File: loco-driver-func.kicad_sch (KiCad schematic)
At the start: 5 parts, among them Q901 BSS138, Q902 BSS138

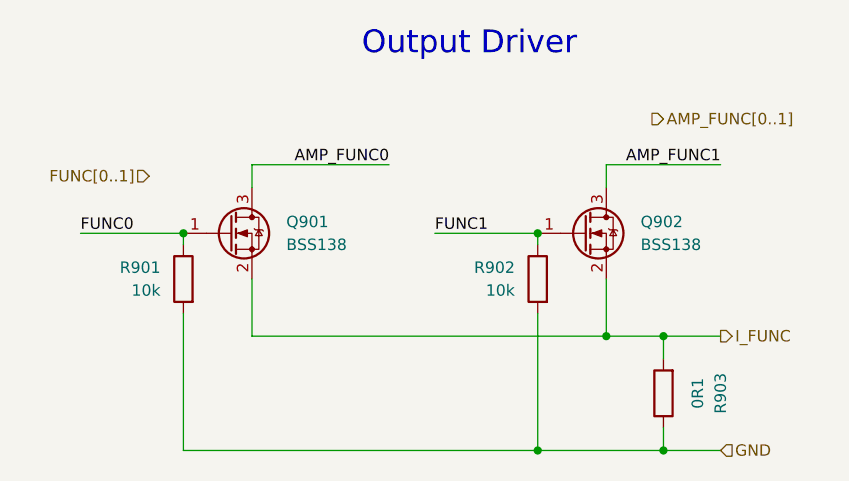
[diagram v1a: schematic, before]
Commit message: Fix - loco-driver-func (ERC)
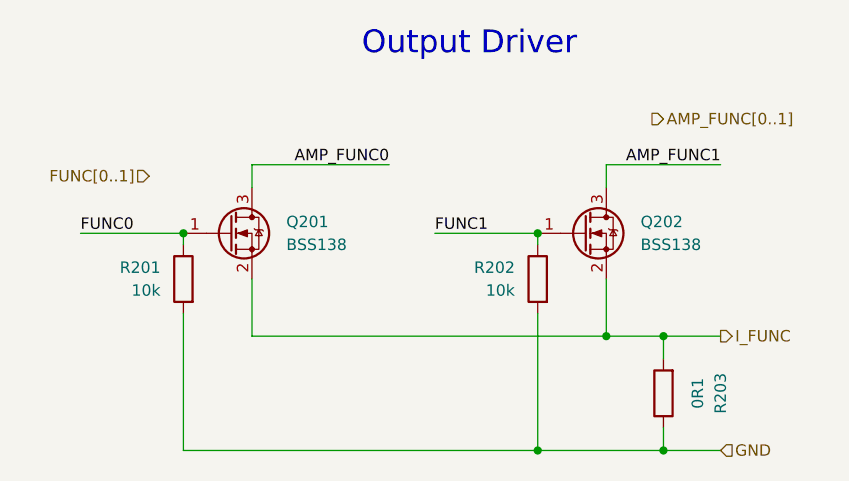
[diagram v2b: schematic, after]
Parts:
- renumbered Q901 to Q201, Q902 to Q202, R901 to R201, R902 to R202, R903 to R203
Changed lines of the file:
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@@
 		(on_board yes)
 		(dnp no)
-		(property "Reference" "R902"
+		(property "Reference" "R202"
 			(at 76.2 59.6899 0)
 			(effects
@@
 			)
 		)
+		(property "Sim.Type" ""
+			(at 78.74 60.96 0)
+			(effects
+				(font
+					(size 1.27 1.27)
+				)
+				(hide yes)
+			)
+		)
 		(pin "2"
 		)
@@
 		)
 		(instances
+			(project "loco-driver-func-test"
+				(path "/05e300d5-f5fa-4357-9552-f348c65b0d1e/d4f38dff-3059-4603-8995-2402d29cae24"
+					(reference "R202")
+					(unit 1)
+				)
+			)
 			(project "xDuinoRails-Thor-M"
 				(path "/fb33ec4e-6596-45d2-a121-8d3475acd69a/e1a52612-70a7-429e-ada6-6f2a698a279c"
@@
 		(on_board yes)
 		(dnp no)
-		(property "Reference" "R903"
+		(property "Reference" "R203"
 			(at 99.06 73.66 90)
 			(effects
@@
 			)
 		)
+		(property "Sim.Type" ""
+			(at 92.71 73.66 0)
+			(effects
+				(font
+					(size 1.27 1.27)
+				)
+				(hide yes)
+			)
+		)
 		(pin "2"
 		)
@@
 		)
 		(instances
+			(project "loco-driver-func-test"
+				(path "/05e300d5-f5fa-4357-9552-f348c65b0d1e/d4f38dff-3059-4603-8995-2402d29cae24"
+					(reference "R203")
+					(unit 1)
+				)
+			)
 			(project "xDuinoRails-Thor-M"
 				(path "/fb33ec4e-6596-45d2-a121-8d3475acd69a/e1a52612-70a7-429e-ada6-6f2a698a279c"
@@
 		(on_board yes)
 		(dnp no)
-		(property "Reference" "R901"
+		(property "Reference" "R201"
 			(at 36.83 59.6899 0)
 			(effects
@@
 			)
 		)
+		(property "Sim.Type" ""
+			(at 39.37 60.96 0)
+			(effects
+				(font
+					(size 1.27 1.27)
+				)
+				(hide yes)
+			)
+		)
 		(pin "2"
 		)
@@
 		)
 		(instances
+			(project "loco-driver-func-test"
+				(path "/05e300d5-f5fa-4357-9552-f348c65b0d1e/d4f38dff-3059-4603-8995-2402d29cae24"
+					(reference "R201")
+					(unit 1)
+				)
+			)
 			(project "xDuinoRails-Thor-M"
 				(path "/fb33ec4e-6596-45d2-a121-8d3475acd69a/e1a52612-70a7-429e-ada6-6f2a698a279c"
@@
 		(dnp no)
 		(fields_autoplaced yes)
-		(property "Reference" "Q901"
+		(property "Reference" "Q201"
 			(at 50.8 54.6099 0)
 			(effects
@@
 			)
 		)
+		(property "Sim.Type" ""
+			(at 44.45 55.88 0)
+			(effects
+				(font
+					(size 1.27 1.27)
+				)
+				(hide yes)
+			)
+		)
 		(pin "1"
 		)
@@
 		)
 		(instances
+			(project "loco-driver-func-test"
+				(path "/05e300d5-f5fa-4357-9552-f348c65b0d1e/d4f38dff-3059-4603-8995-2402d29cae24"
+					(reference "Q201")
+					(unit 1)
+				)
+			)
 			(project "xDuinoRails-Thor-M"
 				(path "/fb33ec4e-6596-45d2-a121-8d3475acd69a/e1a52612-70a7-429e-ada6-6f2a698a279c"
@@
 		(dnp no)
 		(fields_autoplaced yes)
-		(property "Reference" "Q902"
+		(property "Reference" "Q202"
 			(at 90.17 54.6099 0)
 			(effects
@@
 			)
 		)
+		(property "Sim.Type" ""
+			(at 83.82 55.88 0)
+			(effects
+				(font
+					(size 1.27 1.27)
+				)
+				(hide yes)
+			)
+		)
 		(pin "1"
 		)
@@
 		)
 		(instances
+			(project "loco-driver-func-test"
+				(path "/05e300d5-f5fa-4357-9552-f348c65b0d1e/d4f38dff-3059-4603-8995-2402d29cae24"
+					(reference "Q202")
+					(unit 1)
+				)
+			)
 			(project "xDuinoRails-Thor-M"
 				(path "/fb33ec4e-6596-45d2-a121-8d3475acd69a/e1a52612-70a7-429e-ada6-6f2a698a279c"
